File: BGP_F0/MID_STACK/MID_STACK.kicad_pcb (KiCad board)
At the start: 2 copper layers, 20 x 26 mm, 7 parts, among them P1 CONN_01X04, P2 CONN_01X09

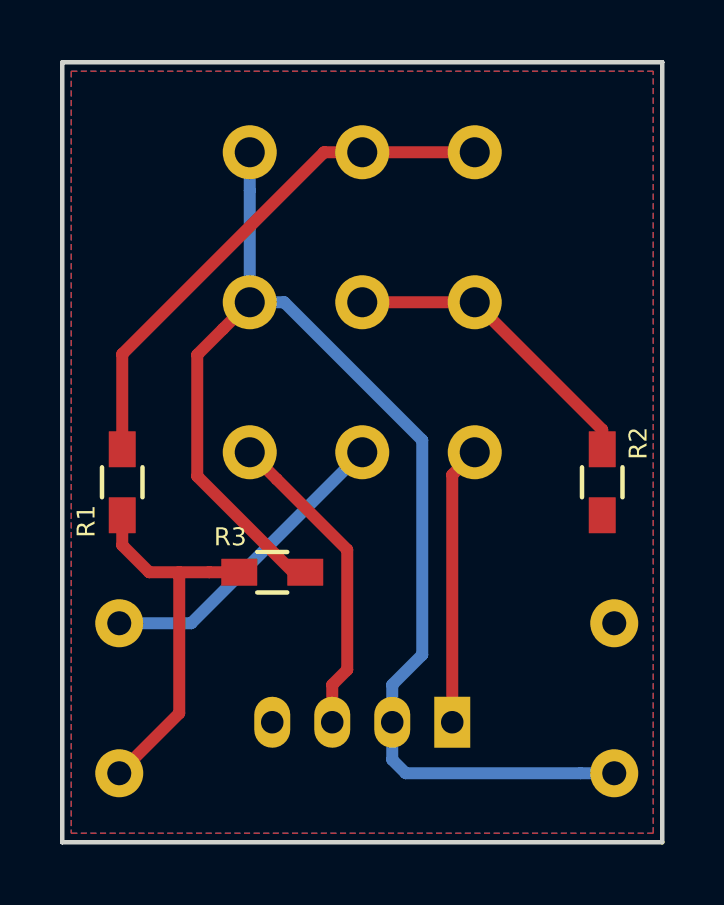
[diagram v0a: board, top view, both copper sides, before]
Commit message: F0 Pot Wiring reversed after testing
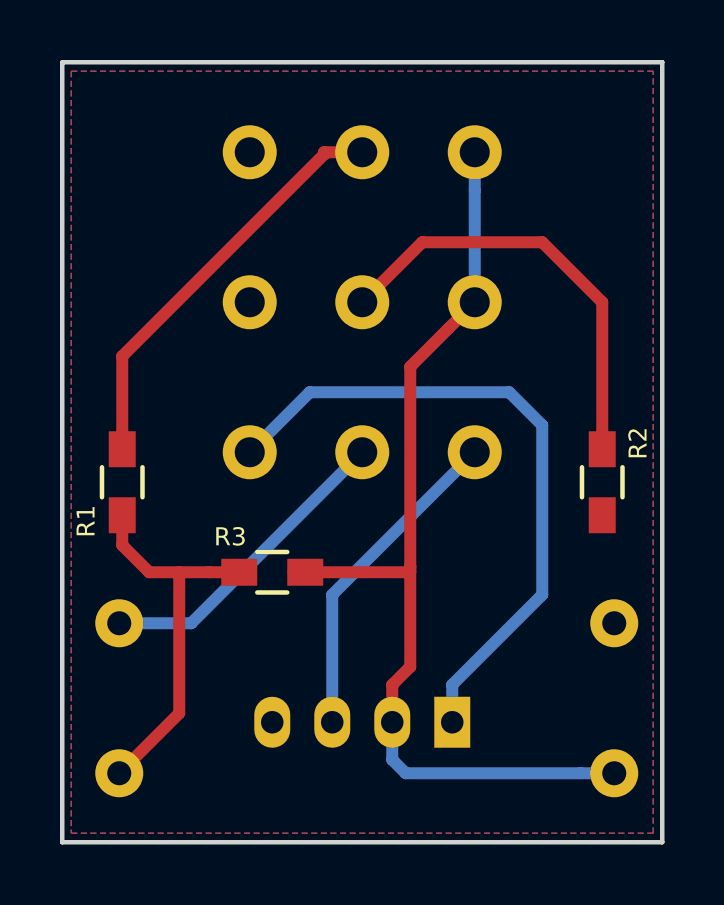
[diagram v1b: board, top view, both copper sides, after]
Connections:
- P2 pad 1: /F1_1 -> Net-(P2-Pad1)
- P2 pad 3: /F1_2 -> /F1_1
- P2 pad 4: /F1_1 -> Net-(P2-Pad4)
- P2 pad 6: /F2_2 -> /F1_1
- P2 pad 7: /MID_O -> /MID_I
- P2 pad 9: /MID_I -> /MID_O
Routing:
- net /MID_I: track 9.31 -> 22.2 mm
- net /F1_1: track 42.8 -> 33.1 mm
- net /F2_2: track 10.4 -> 14.6 mm
- net /F1_2: track 17.7 -> 14.0 mm
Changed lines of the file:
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@@
 (kicad_pcb (version 4) (host pcbnew 4.0.7)
   (general
-    (links 15)
-    (no_connects 0)
+    (links 13)
+    (no_connects 8)
     (area 164.924999 91.924999 185.075001 118.075001)
     (thickness 1.6)
     (drawings 8)
-    (tracks 40)
+    (tracks 41)
     (zones 0)
     (modules 7)
-    (nets 9)
+    (nets 11)
   )
   (page A4)
@@
   (net 7 /F1_2)
   (net 8 /F2_2)
+  (net 9 "Net-(P2-Pad1)")
+  (net 10 "Net-(P2-Pad4)")
   (net_class Default "This is the default net class."
     (clearance 0.3)
@@
     (add_net /Vref)
     (add_net "Net-(C1-Pad2)")
+    (add_net "Net-(P2-Pad1)")
+    (add_net "Net-(P2-Pad4)")
   )
   (net_class PWR ""
@@
     (fp_line (start 2.05 10.7) (end -15.15 10.7) (layer B.CrtYd) (width 0.05))
     (pad 3 thru_hole circle (at 0 7.5 90) (size 1.8 1.8) (drill 1) (layers *.Cu *.Mask)
-      (net 7 /F1_2))
+      (net 3 /F1_1))
     (pad 2 thru_hole circle (at 0 3.75 90) (size 1.8 1.8) (drill 1) (layers *.Cu *.Mask)
       (net 7 /F1_2))
     (pad 1 thru_hole circle (at 0 0 90) (size 1.8 1.8) (drill 1) (layers *.Cu *.Mask)
+      (net 9 "Net-(P2-Pad1)"))
+    (pad 6 thru_hole circle (at -5 7.5 90) (size 1.8 1.8) (drill 1) (layers *.Cu *.Mask)
       (net 3 /F1_1))
-    (pad 6 thru_hole circle (at -5 7.5 90) (size 1.8 1.8) (drill 1) (layers *.Cu *.Mask)
-      (net 8 /F2_2))
     (pad 5 thru_hole circle (at -5 3.75 90) (size 1.8 1.8) (drill 1) (layers *.Cu *.Mask)
       (net 8 /F2_2))
     (pad 4 thru_hole circle (at -5 0 90) (size 1.8 1.8) (drill 1) (layers *.Cu *.Mask)
-      (net 3 /F1_1))
+      (net 10 "Net-(P2-Pad4)"))
     (pad 7 thru_hole circle (at -10 0 90) (size 1.8 1.8) (drill 1) (layers *.Cu *.Mask)
-      (net 6 /MID_O))
+      (net 5 /MID_I))
     (pad 8 thru_hole circle (at -10 3.75 90) (size 1.8 1.8) (drill 1) (layers *.Cu *.Mask)
       (net 1 /VOL2))
     (pad 9 thru_hole circle (at -10 7.5 90) (size 1.8 1.8) (drill 1) (layers *.Cu *.Mask)
-      (net 5 /MID_I))
+      (net 6 /MID_O))
     (model Potentiometers.3dshapes/Potentiometer_Alps_RK097_Double_Vertical.wrl
       (at (xyz 0 0 0))
@@
   (segment (start 169.9 109) (end 170.9 109) (width 0.4) (layer F.Cu) (net 2))
   (segment (start 167 108.1) (end 167.9 109) (width 0.4) (layer F.Cu) (net 2))
+  (segment (start 178.75 95) (end 178.75 96.272792) (width 0.4) (layer B.Cu) (net 3))
+  (segment (start 178.75 96.272792) (end 178.75 100) (width 0.4) (layer B.Cu) (net 3))
+  (segment (start 176.6 109) (end 176.6 108.8) (width 0.4) (layer F.Cu) (net 3))
+  (segment (start 176.6 108.8) (end 176.6 102.15) (width 0.4) (layer F.Cu) (net 3))
+  (segment (start 176 114) (end 176 112.75) (width 0.4) (layer F.Cu) (net 3))
+  (segment (start 176.6 112.15) (end 176.6 108.8) (width 0.4) (layer F.Cu) (net 3))
+  (segment (start 176 112.75) (end 176.6 112.15) (width 0.4) (layer F.Cu) (net 3))
+  (segment (start 173.1 109) (end 176.6 109) (width 0.4) (layer F.Cu) (net 3))
+  (segment (start 176.6 102.15) (end 177.850001 100.899999) (width 0.4) (layer F.Cu) (net 3))
+  (segment (start 177.850001 100.899999) (end 178.75 100) (width 0.4) (layer F.Cu) (net 3))
   (segment (start 173.1 109) (end 172.7 109) (width 0.4) (layer F.Cu) (net 3))
-  (segment (start 172.7 109) (end 169.5 105.8) (width 0.4) (layer F.Cu) (net 3))
-  (segment (start 169.5 105.8) (end 169.5 101.75) (width 0.4) (layer F.Cu) (net 3))
-  (segment (start 169.5 101.75) (end 170.350001 100.899999) (width 0.4) (layer F.Cu) (net 3))
-  (segment (start 170.350001 100.899999) (end 171.25 100) (width 0.4) (layer F.Cu) (net 3))
-  (segment (start 177 111.75) (end 177 104.6) (width 0.4) (layer B.Cu) (net 3))
-  (segment (start 177 104.6) (end 172.4 100) (width 0.4) (layer B.Cu) (net 3))
-  (segment (start 172.4 100) (end 171.25 100) (width 0.4) (layer B.Cu) (net 3))
-  (segment (start 176 114) (end 176 112.75) (width 0.4) (layer B.Cu) (net 3))
-  (segment (start 176 112.75) (end 177 111.75) (width 0.4) (layer B.Cu) (net 3))
   (segment (start 176 114) (end 176 115.25) (width 0.4) (layer B.Cu) (net 3))
   (segment (start 176 115.25) (end 176.45 115.7) (width 0.4) (layer B.Cu) (net 3))
   (segment (start 176.45 115.7) (end 182.26863 115.7) (width 0.4) (layer B.Cu) (net 3))
   (segment (start 182.26863 115.7) (end 183.4 115.7) (width 0.4) (layer B.Cu) (net 3))
-  (segment (start 171.25 95) (end 171.25 96.272792) (width 0.4) (layer B.Cu) (net 3))
-  (segment (start 171.25 96.272792) (end 171.25 100) (width 0.4) (layer B.Cu) (net 3))
-  (segment (start 178 114) (end 178 105.75) (width 0.4) (layer F.Cu) (net 5))
-  (segment (start 178 105.75) (end 178.75 105) (width 0.4) (layer F.Cu) (net 5))
-  (segment (start 174 114) (end 174 112.75) (width 0.4) (layer F.Cu) (net 6))
-  (segment (start 174.5 112.25) (end 174.5 108.25) (width 0.4) (layer F.Cu) (net 6))
-  (segment (start 174 112.75) (end 174.5 112.25) (width 0.4) (layer F.Cu) (net 6))
-  (segment (start 174.5 108.25) (end 172.149999 105.899999) (width 0.4) (layer F.Cu) (net 6))
-  (segment (start 172.149999 105.899999) (end 171.25 105) (width 0.4) (layer F.Cu) (net 6))
+  (segment (start 171.25 105) (end 173.25 103) (width 0.4) (layer B.Cu) (net 5))
+  (segment (start 173.25 103) (end 179.9 103) (width 0.4) (layer B.Cu) (net 5))
+  (segment (start 179.9 103) (end 181 104.1) (width 0.4) (layer B.Cu) (net 5))
+  (segment (start 181 104.1) (end 181 109.75) (width 0.4) (layer B.Cu) (net 5))
+  (segment (start 181 109.75) (end 178 112.75) (width 0.4) (layer B.Cu) (net 5))
+  (segment (start 178 112.75) (end 178 114) (width 0.4) (layer B.Cu) (net 5))
+  (segment (start 178.75 105) (end 174 109.75) (width 0.4) (layer B.Cu) (net 6))
+  (segment (start 174 109.75) (end 174 114) (width 0.4) (layer B.Cu) (net 6))
   (segment (start 174 114.25) (end 174 114) (width 0.4) (layer F.Cu) (net 6))
-  (segment (start 175 95) (end 178.75 95) (width 0.4) (layer F.Cu) (net 7))
-  (segment (start 167 104.9) (end 167 101.727208) (width 0.4) (layer F.Cu) (net 7))
-  (segment (start 167 101.727208) (end 173.727208 95) (width 0.4) (layer F.Cu) (net 7))
+  (segment (start 167 104.9) (end 167 101.8) (width 0.4) (layer F.Cu) (net 7))
+  (segment (start 167 101.8) (end 173.727208 95.072792) (width 0.4) (layer F.Cu) (net 7))
+  (segment (start 173.727208 95.072792) (end 173.727208 95) (width 0.4) (layer F.Cu) (net 7))
   (segment (start 173.727208 95) (end 175 95) (width 0.4) (layer F.Cu) (net 7))
-  (segment (start 178.75 100) (end 183 104.25) (width 0.4) (layer F.Cu) (net 8))
-  (segment (start 183 104.25) (end 183 104.9) (width 0.4) (layer F.Cu) (net 8))
-  (segment (start 175 100) (end 178.75 100) (width 0.4) (layer F.Cu) (net 8))
+  (segment (start 183 104.9) (end 183 100) (width 0.4) (layer F.Cu) (net 8))
+  (segment (start 183 100) (end 181 98) (width 0.4) (layer F.Cu) (net 8))
+  (segment (start 181 98) (end 177 98) (width 0.4) (layer F.Cu) (net 8))
+  (segment (start 177 98) (end 175 100) (width 0.4) (layer F.Cu) (net 8))
   (zone (net 4) (net_name /Vref) (layer F.Cu) (hatch edge 0.508)
     (connect_pads (clearance 0.3))

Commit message: F0 Conn changes
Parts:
- moved P1 6.00 mm to (172.0, 114.0), turned to 0 degrees
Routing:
- net /MID_I: track 22.2 -> 9.31 mm
- net /VOL2: track 10.5 -> 15.0 mm
- net /MID_O: track 11.2 -> 10.1 mm
- removed copper zone on B.Cu, net (none)
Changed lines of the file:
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@@
   (general
     (links 13)
-    (no_connects 8)
+    (no_connects 5)
     (area 164.924999 91.924999 185.075001 118.075001)
     (thickness 1.6)
     (drawings 8)
-    (tracks 41)
+    (tracks 39)
     (zones 0)
     (modules 7)
@@
   )
   (module Connectors_JST:JST_PH_B4B-PH-K_04x2.00mm_Straight (layer B.Cu)
-    (at 178 114 180)
+    (at 172 114)
     (descr "JST PH series connector, B4B-PH-K, top entry type, through hole, Datasheet: http://www.jst-mfg.com/product/pdf/eng/ePH.pdf")
     (tags "connector jst ph")
-    (fp_text reference P1 (at 7.6 2.3 180) (layer B.SilkS)
-      (effects (font (size 0.6 0.6) (thickness 0.15)) (justify mirror))
-    )
-    (fp_text value CONN_01X04 (at 3 -3.8 180) (layer B.Fab) hide
+    (fp_text reference P1 (at 7.6 2.3) (layer B.SilkS)
+      (effects (font (size 0.6 0.6) (thickness 0.15)) (justify mirror))
+    )
+    (fp_text value CONN_01X04 (at 3 -3.8) (layer B.Fab) hide
       (effects (font (size 0.6 0.6) (thickness 0.15)) (justify mirror))
     )
@@
     (fp_line (start 8.45 -3.3) (end 8.45 2.2) (layer B.CrtYd) (width 0.05))
     (fp_line (start 8.45 2.2) (end -2.45 2.2) (layer B.CrtYd) (width 0.05))
-    (fp_text user %R (at 3 -1.5 180) (layer B.Fab) hide
-      (effects (font (size 0.6 0.6) (thickness 0.15)) (justify mirror))
-    )
-    (pad 1 thru_hole rect (at 0 0 180) (size 1.2 1.7) (drill 0.75) (layers *.Cu *.Mask)
+    (fp_text user %R (at 3 -1.5) (layer B.Fab) hide
+      (effects (font (size 0.6 0.6) (thickness 0.15)) (justify mirror))
+    )
+    (pad 1 thru_hole rect (at 0 0) (size 1.2 1.7) (drill 0.75) (layers *.Cu *.Mask)
       (net 5 /MID_I))
-    (pad 2 thru_hole oval (at 2 0 180) (size 1.2 1.7) (drill 0.75) (layers *.Cu *.Mask)
+    (pad 2 thru_hole oval (at 2 0) (size 1.2 1.7) (drill 0.75) (layers *.Cu *.Mask)
       (net 3 /F1_1))
-    (pad 3 thru_hole oval (at 4 0 180) (size 1.2 1.7) (drill 0.75) (layers *.Cu *.Mask)
+    (pad 3 thru_hole oval (at 4 0) (size 1.2 1.7) (drill 0.75) (layers *.Cu *.Mask)
       (net 6 /MID_O))
-    (pad 4 thru_hole oval (at 6 0 180) (size 1.2 1.7) (drill 0.75) (layers *.Cu *.Mask)
+    (pad 4 thru_hole oval (at 6 0) (size 1.2 1.7) (drill 0.75) (layers *.Cu *.Mask)
       (net 4 /Vref))
     (model ${KISYS3DMOD}/Connectors_JST.3dshapes/JST_PH_B4B-PH-K_04x2.00mm_Straight.wrl
@@
   (gr_line (start 165 92) (end 165 118) (layer Edge.Cuts) (width 0.15))
   (gr_line (start 185 92) (end 165 92) (layer Edge.Cuts) (width 0.15))
-  (segment (start 166.9 110.7) (end 169.3 110.7) (width 0.4) (layer B.Cu) (net 1))
-  (segment (start 169.3 110.7) (end 175 105) (width 0.4) (layer B.Cu) (net 1))
+  (segment (start 169.7 103) (end 173 103) (width 0.4) (layer B.Cu) (net 1))
+  (segment (start 173 103) (end 175 105) (width 0.4) (layer B.Cu) (net 1))
+  (segment (start 166.9 105.8) (end 169.7 103) (width 0.4) (layer B.Cu) (net 1))
+  (segment (start 166.9 110.7) (end 166.9 105.8) (width 0.4) (layer B.Cu) (net 1))
   (segment (start 167.9 109) (end 168.9 109) (width 0.4) (layer F.Cu) (net 2))
   (segment (start 168.9 109) (end 169.9 109) (width 0.4) (layer F.Cu) (net 2))
@@
   (segment (start 169.9 109) (end 170.9 109) (width 0.4) (layer F.Cu) (net 2))
   (segment (start 167 108.1) (end 167.9 109) (width 0.4) (layer F.Cu) (net 2))
+  (segment (start 173.1 109) (end 173.4 109) (width 0.4) (layer F.Cu) (net 3))
+  (segment (start 173.4 109) (end 177 105.4) (width 0.4) (layer F.Cu) (net 3))
+  (segment (start 177 105.4) (end 177 101.75) (width 0.4) (layer F.Cu) (net 3))
+  (segment (start 177 101.75) (end 177.850001 100.899999) (width 0.4) (layer F.Cu) (net 3))
+  (segment (start 177.850001 100.899999) (end 178.75 100) (width 0.4) (layer F.Cu) (net 3))
+  (segment (start 174 114) (end 174 115.25) (width 0.4) (layer F.Cu) (net 3))
+  (segment (start 174 115.25) (end 174.45 115.7) (width 0.4) (layer F.Cu) (net 3))
+  (segment (start 174.45 115.7) (end 182.26863 115.7) (width 0.4) (layer F.Cu) (net 3))
+  (segment (start 182.26863 115.7) (end 183.4 115.7) (width 0.4) (layer F.Cu) (net 3))
+  (segment (start 174 114) (end 174 112.75) (width 0.4) (layer F.Cu) (net 3))
+  (segment (start 174 112.75) (end 173.1 111.85) (width 0.4) (layer F.Cu) (net 3))
+  (segment (start 173.1 111.85) (end 173.1 109) (width 0.4) (layer F.Cu) (net 3))
   (segment (start 178.75 95) (end 178.75 96.272792) (width 0.4) (layer B.Cu) (net 3))
   (segment (start 178.75 96.272792) (end 178.75 100) (width 0.4) (layer B.Cu) (net 3))
-  (segment (start 176.6 109) (end 176.6 108.8) (width 0.4) (layer F.Cu) (net 3))
-  (segment (start 176.6 108.8) (end 176.6 102.15) (width 0.4) (layer F.Cu) (net 3))
-  (segment (start 176 114) (end 176 112.75) (width 0.4) (layer F.Cu) (net 3))
-  (segment (start 176.6 112.15) (end 176.6 108.8) (width 0.4) (layer F.Cu) (net 3))
-  (segment (start 176 112.75) (end 176.6 112.15) (width 0.4) (layer F.Cu) (net 3))
-  (segment (start 173.1 109) (end 176.6 109) (width 0.4) (layer F.Cu) (net 3))
-  (segment (start 176.6 102.15) (end 177.850001 100.899999) (width 0.4) (layer F.Cu) (net 3))
-  (segment (start 177.850001 100.899999) (end 178.75 100) (width 0.4) (layer F.Cu) (net 3))
   (segment (start 173.1 109) (end 172.7 109) (width 0.4) (layer F.Cu) (net 3))
-  (segment (start 176 114) (end 176 115.25) (width 0.4) (layer B.Cu) (net 3))
-  (segment (start 176 115.25) (end 176.45 115.7) (width 0.4) (layer B.Cu) (net 3))
-  (segment (start 176.45 115.7) (end 182.26863 115.7) (width 0.4) (layer B.Cu) (net 3))
-  (segment (start 182.26863 115.7) (end 183.4 115.7) (width 0.4) (layer B.Cu) (net 3))
-  (segment (start 171.25 105) (end 173.25 103) (width 0.4) (layer B.Cu) (net 5))
-  (segment (start 173.25 103) (end 179.9 103) (width 0.4) (layer B.Cu) (net 5))
-  (segment (start 179.9 103) (end 181 104.1) (width 0.4) (layer B.Cu) (net 5))
-  (segment (start 181 104.1) (end 181 109.75) (width 0.4) (layer B.Cu) (net 5))
-  (segment (start 181 109.75) (end 178 112.75) (width 0.4) (layer B.Cu) (net 5))
-  (segment (start 178 112.75) (end 178 114) (width 0.4) (layer B.Cu) (net 5))
-  (segment (start 178.75 105) (end 174 109.75) (width 0.4) (layer B.Cu) (net 6))
-  (segment (start 174 109.75) (end 174 114) (width 0.4) (layer B.Cu) (net 6))
-  (segment (start 174 114.25) (end 174 114) (width 0.4) (layer F.Cu) (net 6))
+  (segment (start 172 114) (end 172 107.5) (width 0.4) (layer B.Cu) (net 5))
+  (segment (start 172 107.5) (end 171.25 106.75) (width 0.4) (layer B.Cu) (net 5))
+  (segment (start 171.25 106.75) (end 171.25 105) (width 0.4) (layer B.Cu) (net 5))
+  (segment (start 176 114) (end 176 107.75) (width 0.4) (layer F.Cu) (net 6))
+  (segment (start 176 107.75) (end 178.75 105) (width 0.4) (layer F.Cu) (net 6))
   (segment (start 167 104.9) (end 167 101.8) (width 0.4) (layer F.Cu) (net 7))
   (segment (start 167 101.8) (end 173.727208 95.072792) (width 0.4) (layer F.Cu) (net 7))
@@
     (polygon
       (pts
-        (xy 184.7 92.3) (xy 165.3 92.3) (xy 165.3 117.7) (xy 184.7 117.7)
+        (xy 184.7 117.7) (xy 165.3 117.7) (xy 165.3 92.3) (xy 184.7 92.3)
       )
     )
-  )
-  (zone (net 0) (net_name "") (layer B.Cu) (hatch edge 0.508)
-    (connect_pads (clearance 0.3))
-    (min_thickness 0.3)
-    (fill yes (arc_segments 16) (thermal_gap 0.3) (thermal_bridge_width 0.6))
-    (polygon
-      (pts
-        (xy 184.7 92.3) (xy 165.3 92.3) (xy 165.3 117.7) (xy 184.7 117.7)
-      )
-    )
